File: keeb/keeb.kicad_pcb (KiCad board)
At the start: 2 copper layers, 266.7 x 98.7 mm, 156 parts, among them J1 AudioJack3, J101 USB_C_Receptacle_USB2.0, J102 AVR-ISP-6, SW101 SW_Push, SW102 SW_Push, SW103 SW_Push, SW104 SW_Push, SW105 SW_Push, SW106 SW_Push, SW107 SW_Push, SW108 SW_Push, SW109 SW_Push, SW110 SW_Push, SW111 SW_Push, SW112 SW_Push, SW113 SW_Push, SW114 SW_Push, SW115 SW_Push, SW116 SW_Push, SW117 SW_Push, SW118 SW_Push, SW119 SW_Push, SW120 SW_Push, SW121 SW_Push, SW122 SW_Push, SW123 SW_Push, SW124 SW_Push, SW125 SW_Push, SW126 SW_Push, SW127 SW_Push, SW128 SW_Push, SW129 SW_Push, SW130 SW_Push, SW131 SW_Push, SW132 SW_Push, SW133 SW_Push, SW134 SW_Push, SW135 SW_Push, SW136 SW_Push, SW137 SW_Push, SW138 SW_Push, SW139 SW_Push, SW140 SW_Push, SW141 SW_Push, SW142 SW_Push, SW143 SW_Push, SW144 SW_Push, SW145 SW_Push, SW146 SW_Push, SW147 SW_Push, SW148 SW_Push, SW149 SW_Push, SW150 SW_Push, SW151 SW_Push, SW152 SW_Push, SW153 SW_Push, SW154 SW_Push, SW155 SW_Push, SW156 SW_Push, SW157 SW_Push, SW158 SW_Push, SW159 SW_Push, SW160 SW_Push, SW161 SW_Push, SW162 SW_Push, SW163 SW_Push, SW164 SW_Push, SW165 SW_Push, SW166 SW_Push, U102 ATmega32U4-AU

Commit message: idk
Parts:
- moved R105 1.90 mm to (226.6, 113.3)
- moved R101 1.73 mm to (208.3, 118.2)
- moved R102 1.67 mm to (211.3, 118.2)
- moved C109 1.65 mm to (209.8, 109.9)
- moved F101 1.65 mm to (209.8, 112.1)
- moved J101 1.65 mm to (209.7, 112.9)
- moved RESET 1.52 mm to (229.1, 113.7)
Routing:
- net D-: track 71.0 -> 72.6 mm
- net D+: track 71.6 -> 73.3 mm
- net +5V: track 125.2 -> 126.4 mm
- net ~RESET: track 100.4 -> 101.5 mm
- net GND: track 8.83 -> 9.88 mm, vias 275 -> 280
- net Net-(D107-Pad2): track 11.6 -> 10.9 mm
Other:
- board size 266.7 x 98.7 mm -> 266.7 x 100.3 mm

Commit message: i2c fin
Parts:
- removed J1: AudioJack3, Connector_Audio:Jack_3.5mm_CUI_SJ-3523-SMT_Horizontal
- removed the J101 at (209.7, 112.9)
- added J102: USB_C_Receptacle_USB2.0, unORTHOdox_CF:USB_C_Receptacle_HRO_TYPE-C-31-M-12, B.Cu at (209.7, 112.0)
- added J103: AudioJack4, unORTHOdox_CF:Jack_3.5mm_TIC54-00177_Horizontal, B.Cu at (335.0, 203.5)
- added J104: AudioJack4, unORTHOdox_CF:Jack_3.5mm_TIC54-00177_Horizontal, B.Cu at (85.3, 203.2)
- added R107: 4K7, Resistor_SMD:R_0603_1608Metric_Pad0.98x0.95mm_HandSolder, F.Cu at (78.0, 201.2)
- added R108: 4K7, Resistor_SMD:R_0603_1608Metric_Pad0.98x0.95mm_HandSolder, F.Cu at (79.0, 205.0)
- added R109: 4K7, Resistor_SMD:R_0603_1608Metric_Pad0.98x0.95mm_HandSolder, F.Cu at (339.6, 207.0)
- added R110: 4K7, Resistor_SMD:R_0603_1608Metric_Pad0.98x0.95mm_HandSolder, F.Cu at (341.4, 205.2)
- moved R103 0.51 mm to (208.3, 118.7)
- moved R104 0.51 mm to (211.3, 118.7)
- renumbered C109 to C106, C106 to C107, C107 to C108, C108 to C109, J102 to J101, R105 to R101, R106 to R102, R101 to R103, R102 to R104, R103 to R105, R104 to R106, RESET to SW101, SW101 to SW102, SW102 to SW103, SW103 to SW104, SW104 to SW105, SW105 to SW106, SW106 to SW107, SW107 to SW108, SW108 to SW109, SW109 to SW110, SW110 to SW111, SW111 to SW112, SW112 to SW113, SW113 to SW114, SW114 to SW115, SW115 to SW116, SW116 to SW117, SW117 to SW118, SW118 to SW119, SW119 to SW120, SW120 to SW121, SW121 to SW122, SW122 to SW123, SW123 to SW124, SW124 to SW125, SW125 to SW126, SW126 to SW127, SW127 to SW128, SW128 to SW129, SW129 to SW130, SW130 to SW131, SW131 to SW132, SW132 to SW133, SW133 to SW134, SW134 to SW135, SW135 to SW136, SW136 to SW137, SW137 to SW138, SW138 to SW139, SW139 to SW140, SW140 to SW141, SW141 to SW142, SW142 to SW143, SW143 to SW144, SW144 to SW145, SW145 to SW146, SW146 to SW147, SW147 to SW148, SW148 to SW149, SW149 to SW150, SW150 to SW151, SW151 to SW152, SW152 to SW153, SW153 to SW154, SW154 to SW155, SW155 to SW156, SW156 to SW157, SW157 to SW158, SW158 to SW159, SW159 to SW160, SW160 to SW161, SW161 to SW162, SW162 to SW163, SW163 to SW164, SW164 to SW165, SW165 to SW166, SW166 to SW167, U102 to U101, 16Mhz to Y101
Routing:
- net SCL: track 128.1 -> 286.2 mm, vias 2 -> 5
- net SDA: track 127.2 -> 285.0 mm, vias 2 -> 4
- net +5V: track 126.4 -> 121.2 mm, vias 8 -> 11
- net VBUS: track 11.8 -> 13.1 mm
- net D-: track 72.6 -> 72.0 mm
- net Net-(J2-PadT): vias 0 -> 1
- net GND: vias 280 -> 266

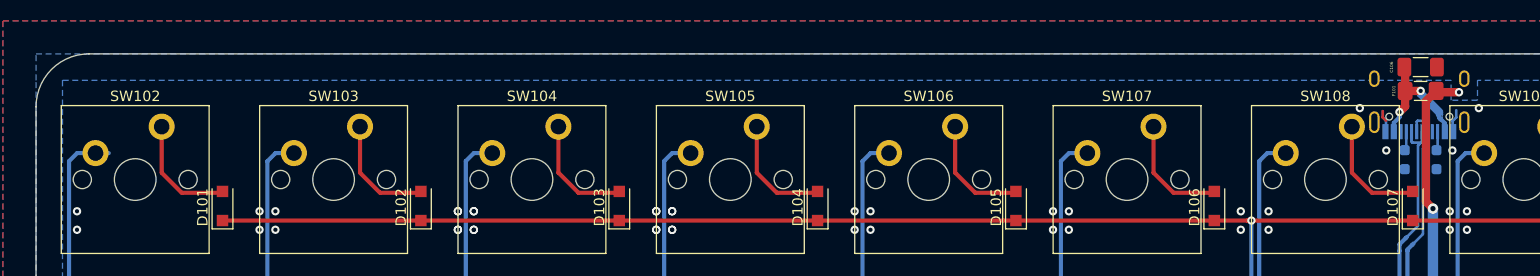
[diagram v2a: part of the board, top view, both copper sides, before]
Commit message: updated bulk decoupling and usb-c routing
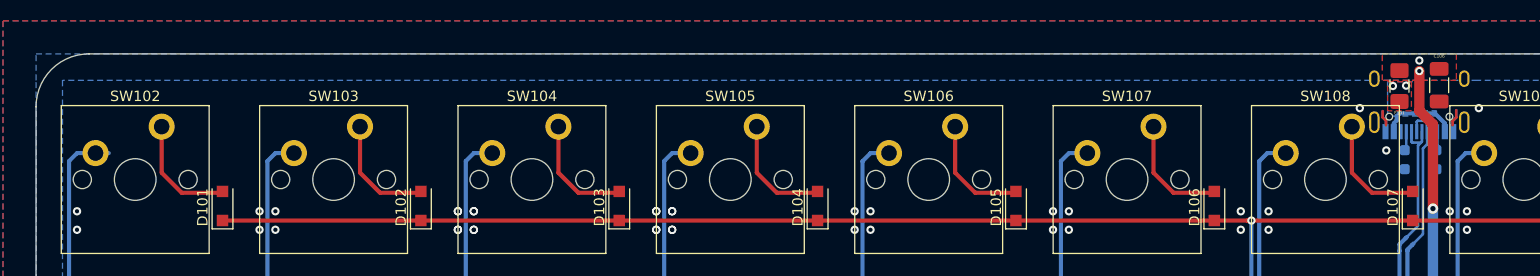
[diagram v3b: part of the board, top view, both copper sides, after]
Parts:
- moved C106 2.49 mm to (211.6, 111.6), turned to 270 degrees
- moved F101 2.09 mm to (207.8, 111.7), turned to 270 degrees
- renumbered J102 to USB-C
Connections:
- C106 pad 1: VBUS -> +5V
- U101 pad 36: Net-(U101-Pad36) -> (no net)
- U101 pad 42: Net-(U101-Pad42) -> (no net)
- USB-C pad A8: Net-(J102-PadA8) -> (no net)
- USB-C pad B8: Net-(J102-PadB8) -> (no net)
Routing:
- net VBUS: track 13.1 -> 7.54 mm
- net GND: track 9.88 -> 11.9 mm, vias 266 -> 265
- net +5V: track 121.2 -> 120.2 mm, vias 11 -> 12
- added copper zone on F.Cu, net +5V
- added copper zone on F.Cu, net VBUS

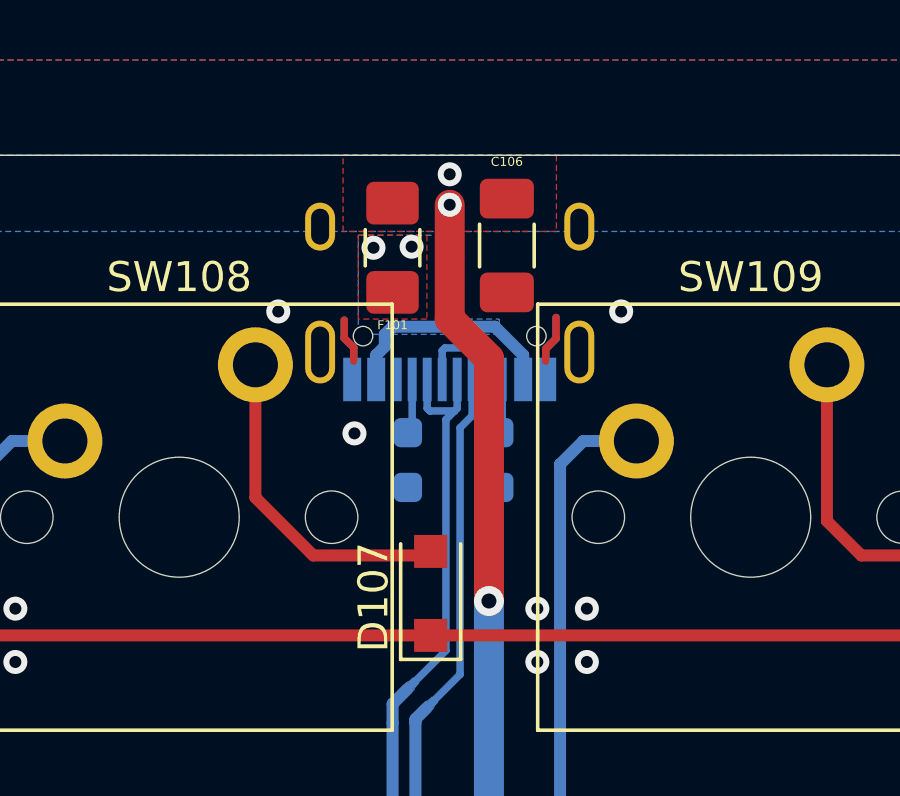
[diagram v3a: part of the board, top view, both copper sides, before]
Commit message: USB power pour alignment
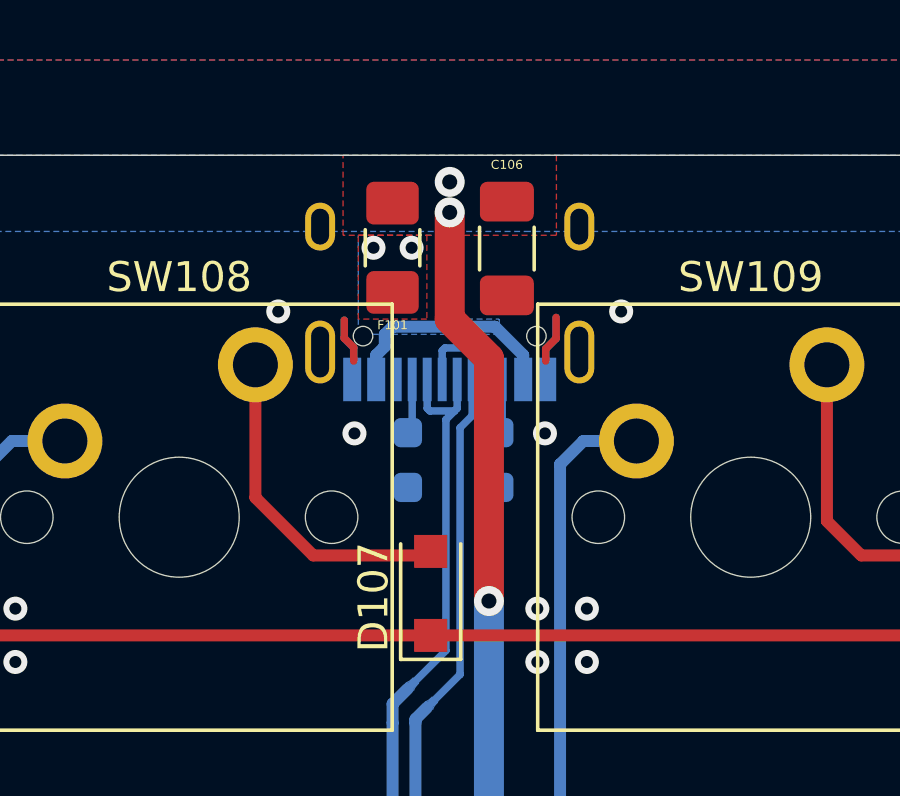
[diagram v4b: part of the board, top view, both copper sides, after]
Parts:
- moved C106 0.10 mm to (211.6, 111.7)
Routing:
- net GND: vias 265 -> 266

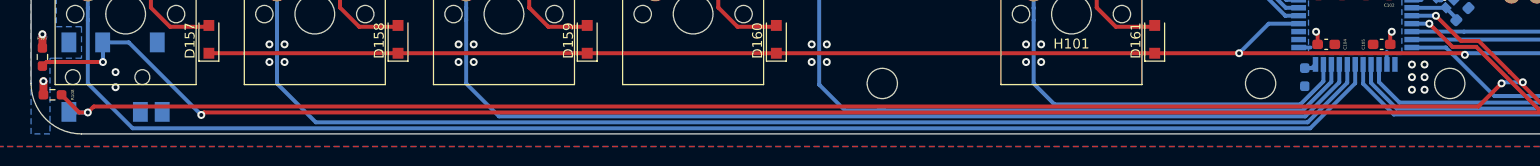
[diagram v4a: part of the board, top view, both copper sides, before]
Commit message: update I2C routing
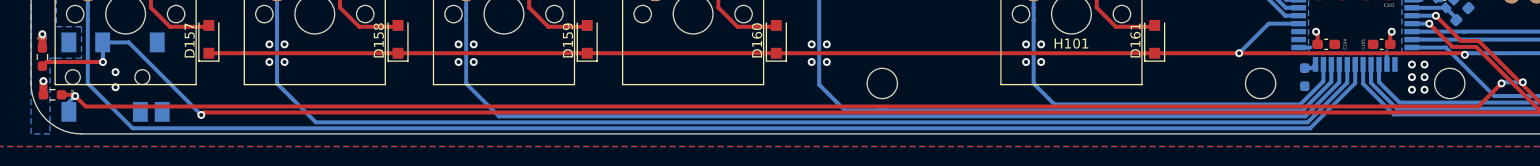
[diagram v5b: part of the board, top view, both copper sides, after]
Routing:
- net SCL: track 286.2 -> 285.7 mm
